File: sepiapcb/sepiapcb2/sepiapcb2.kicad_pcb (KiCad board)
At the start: 2 copper layers, 98.1 x 75.2 mm, 5 parts, among them SW1 SW_DPDT_x2

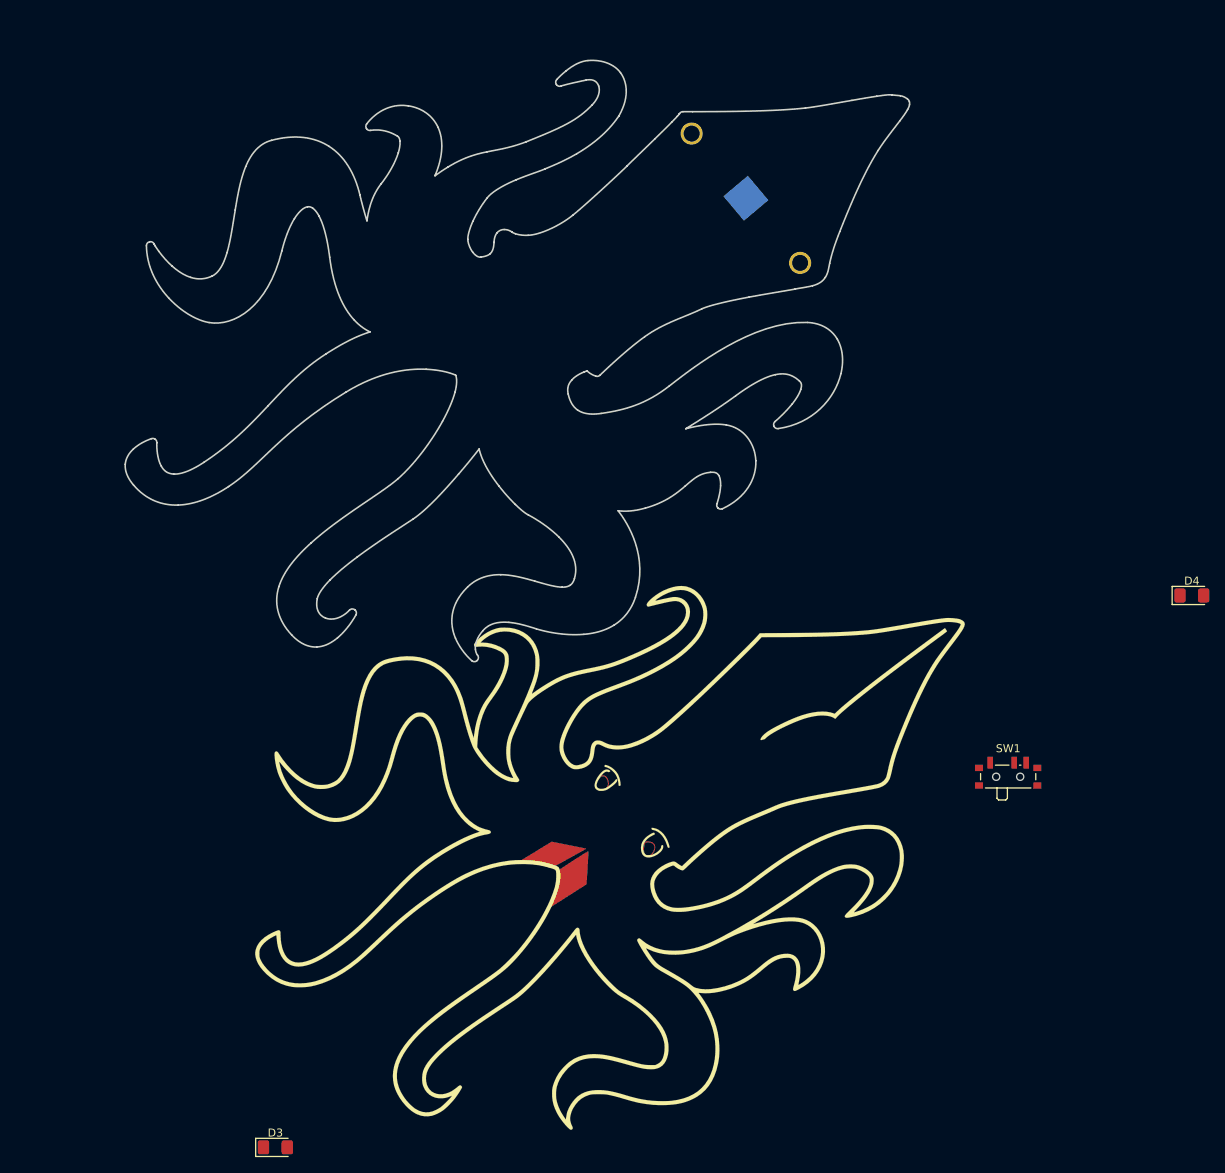
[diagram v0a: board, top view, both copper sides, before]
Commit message: Sepia footprint also enlarged
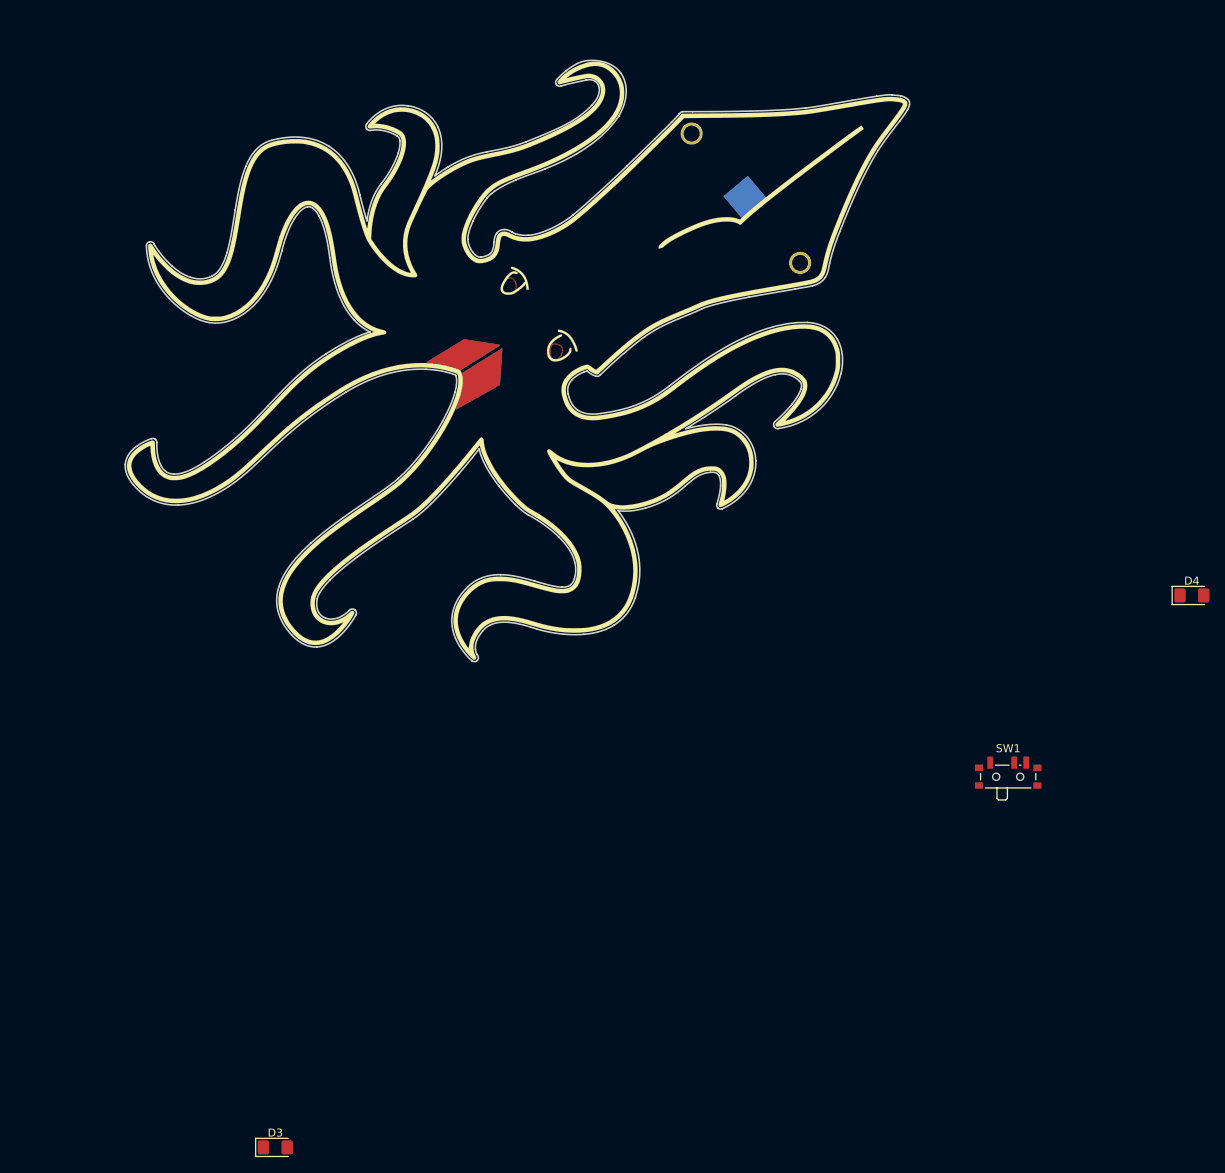
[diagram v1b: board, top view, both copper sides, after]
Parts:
- D1: footprint sepiapcb:sepia_footrprint_pcb -> sepiapcb:sepia_footprint_enlarged_pcb
- moved D1 63.2 mm to (75.8, 67.9)

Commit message: Enlarged sepia almost done
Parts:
- D3, D4: footprint LED_SMD:LED_1206_3216Metric_Pad1.42x1.75mm_HandSolder -> sepiapcb:LED_1206_3216Metric_ReverseMount_NoHole1.8x2.4mm; moved to B.Cu
- SW1: moved to B.Cu
- moved D3 105.4 mm to (80.8, 63.4)
- moved D4 93.5 mm to (75.2, 55.2)
- moved SW1 85.3 mm to (84.8, 49.0), turned to 35 degrees
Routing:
- net +3V0: track 0.00 -> 48.2 mm
- net Net-(D1-Pad1): track 0.00 -> 36.0 mm
- net GND: track 0.00 -> 32.9 mm, vias 0 -> 4
- added copper zone on B.Cu, net GND
- added copper zone on F.Cu, net GND
